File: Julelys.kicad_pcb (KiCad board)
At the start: 4 copper layers, 60 x 53 mm, 85 parts, among them J1 Conn_02x13_Top_Bottom, J10 B3B-XH-A, J11 B3B-XH-A, J12 Conn_01x03_Pin, J2 Conn_01x13, J3 Conn_02x06_Odd_Even, J4 B3B-XH-A, J5 B3B-XH-A, J6 B3B-XH-A, J7 B3B-XH-A, J8 B3B-XH-A, J9 B3B-XH-A, P1 USB_C_Receptacle_USB2.0, SW1 SW_Push, SW2 SW_Push, U1 ESP32-C3-WROOM-02, U2 74HC4051, U3 AMS1117-3.3, U4 BC847BDW1T1G, U5 CP2102N-A02-GQFN28, U6 74AHCT1G125, U7 74AHCT1G125, U8 74AHCT1G125, U9 74AHCT1G125

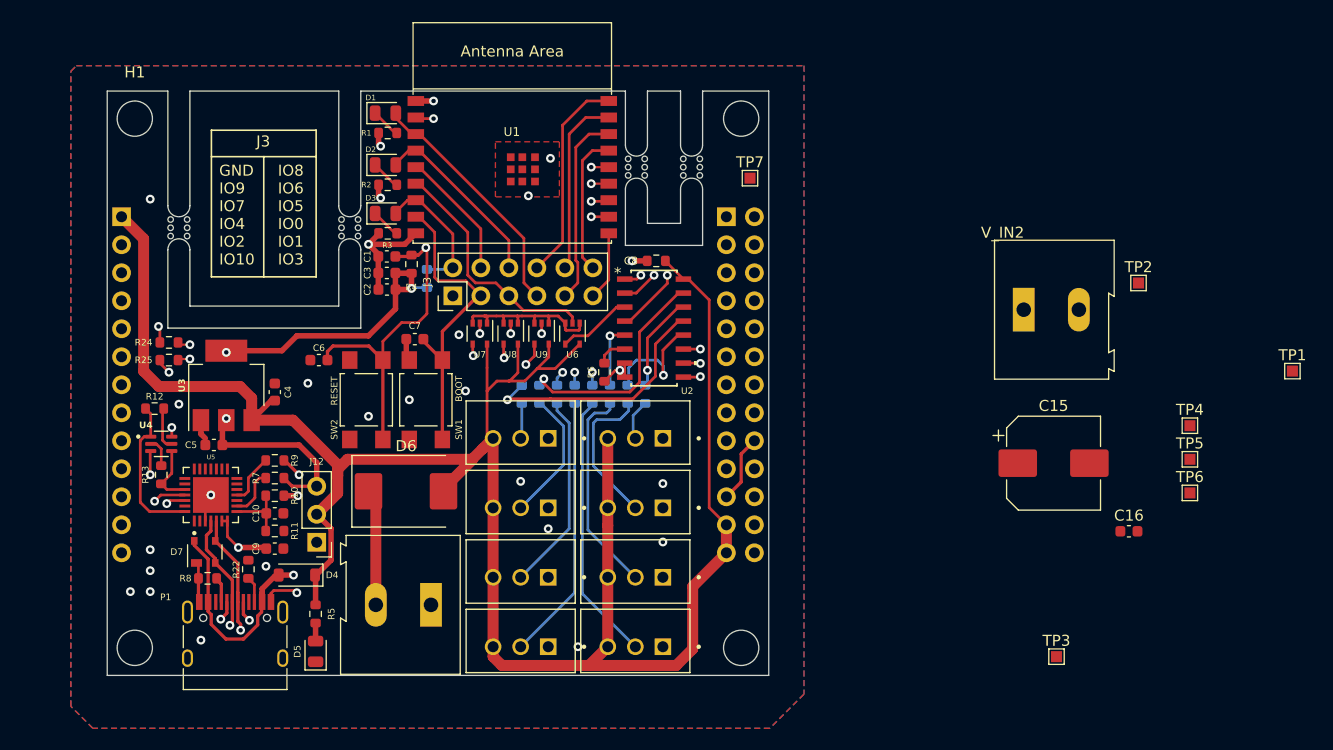
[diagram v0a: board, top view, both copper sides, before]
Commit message: Start v4 layout on Raspberry Pi HAT outline
Clear the v3.1 layout down to a 65x56 mm HAT board outline with the four
M3 mounting holes, ready for fresh placement. Update the schematic and
CLAUDE.md for the Raspberry Pi 40-pin header.

Co-Authored-By: Claude Opus 5.5 <noreply@anthropic.com>
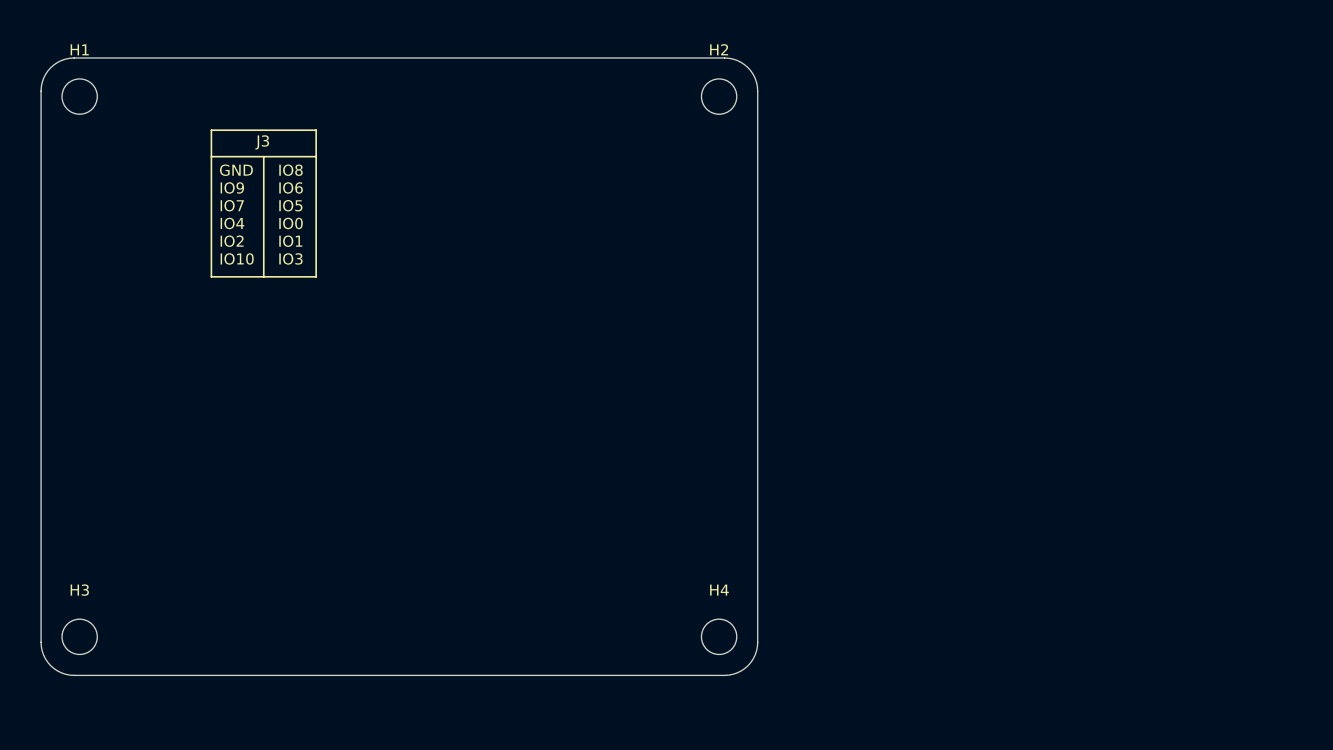
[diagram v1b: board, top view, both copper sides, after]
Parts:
- removed C1: 1uf/16V, Capacitor_SMD:C_0603_1608Metric
- removed C10: 1uF/16V(10%), Capacitor_SMD:C_0603_1608Metric
- removed C15: 470uF, Capacitor_SMD:CP_Elec_8x10
- removed C16: 100nF, Capacitor_SMD:C_0603_1608Metric
- removed C2, C4, C5: 10uf, Capacitor_SMD:C_0603_1608Metric
- removed C3, C6, C7: 0.1uf, Capacitor_SMD:C_0603_1608Metric
- removed C8: 100nf, Resistor_SMD:R_0603_1608Metric
- removed C9: 10uF/25V(20%), Capacitor_SMD:C_0603_1608Metric
- removed D1, D2, D3: LED RED, LED_SMD:LED_0805_2012Metric
- removed D4: 1N5819HW-7-F, Diode_SMD:D_SOD-123
- removed D5: LED GREEN, LED_SMD:LED_0805_2012Metric
- removed D6: SS34, Diode_SMD:D_SMC
- removed D7: SP0503BAHT, Package_TO_SOT_SMD:SOT-143
- removed J1: Conn_02x13_Top_Bottom, Connector_PinSocket_2.54mm:PinSocket_2x13_P2.54mm_Vertical
- removed J10, J11, J4, J5, J6, J7, J8, J9: B3B-XH-A, Connector:JST_B3B-XH-A
- removed J12: Conn_01x03_Pin, Connector_PinHeader_2.54mm:PinHeader_1x03_P2.54mm_Vertical
- removed J2: Conn_01x13, Connector_PinSocket_2.54mm:PinSocket_1x13_P2.54mm_Vertical
- removed J3: Conn_02x06_Odd_Even, Connector_PinHeader_2.54mm:PinHeader_2x06_P2.54mm_Vertical
- removed P1: USB_C_Receptacle_USB2.0, Connector_USB:USB_C_Receptacle_HRO_TYPE-C-31-M-12
- removed R1, R2, R3: 270, Resistor_SMD:R_0603_1608Metric
- removed R10: 22.1K, Resistor_SMD:R_0603_1608Metric
- removed R11: 47.5K, Resistor_SMD:R_0603_1608Metric
- removed R12, R13: 10k, Resistor_SMD:R_0603_1608Metric
- removed R14, R15, R16, R17, R18, R19, R20, R21: 330, Resistor_SMD:R_0603_1608Metric
- removed R22, R8: 5.1K, Resistor_SMD:R_0603_1608Metric
- removed R23, R4, R6, R9: 10K, Resistor_SMD:R_0603_1608Metric
- removed R24, R25: 22, Resistor_SMD:R_0603_1608Metric
- removed R5: 5k1, Resistor_SMD:R_0603_1608Metric
- removed R7: 1K, Resistor_SMD:R_0603_1608Metric
- removed SW1, SW2: SW_Push, Button_Switch_SMD:SW_SPST_TL3305A
- removed TP1: 5V, TestPoint:TestPoint_Pad_1.0x1.0mm
- removed TP2: GND, TestPoint:TestPoint_Pad_1.0x1.0mm
- removed TP3: 3.3V, TestPoint:TestPoint_Pad_1.0x1.0mm
- removed TP4: MOSI, TestPoint:TestPoint_Pad_1.0x1.0mm
- removed TP5: MISO, TestPoint:TestPoint_Pad_1.0x1.0mm
- removed TP6: CLK, TestPoint:TestPoint_Pad_1.0x1.0mm
- removed TP7: CS, TestPoint:TestPoint_Pad_1.0x1.0mm
- removed U1: ESP32-C3-WROOM-02, PCM_Espressif:ESP32-C3-WROOM-02
- removed U2: 74HC4051, 74HC4051D_FOOTPRINT:SOIC16_TOS
- removed U3: AMS1117-3.3, Package_TO_SOT_SMD:SOT-223-3_TabPin2
- removed U4: BC847BDW1T1G, Transistor_Power_Module:SOT65P210X110-6N
- removed U5: CP2102N-A02-GQFN28, Connector_USB:QFN50P500X500X80-29N
- removed U6, U7, U8, U9: 74AHCT1G125, Package_TO_SOT_SMD:SOT-353_SC-70-5
- removed V_IN1, V_IN2: 5V, TerminalBlock:TerminalBlock_Altech_AK300-2_P5.00mm
- removed mouse-bite-2mm-slot (x4): VAL**, footprints:mouse-bite-2mm-slot
- moved H1 5.39 mm to (23.5, 15.5)
- moved H3 5.10 mm to (23.5, 64.5)
- moved H2 2.83 mm to (81.5, 15.5)
- moved H4 2.24 mm to (81.5, 64.5)
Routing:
- net +5V: track 210.7 -> 0.00 mm
- net TXD: track 117.8 -> 0.00 mm, vias 2 -> 0
- net RXD: track 112.6 -> 0.00 mm, vias 2 -> 0
- net +3.3V: track 86.6 -> 0.00 mm, vias 5 -> 0
- net CHIP_UP: track 79.3 -> 0.00 mm, vias 3 -> 0
- net IO9: track 73.2 -> 0.00 mm, vias 1 -> 0
- net GND: track 58.2 -> 0.00 mm, vias 28 -> 0
- net USB_D+: track 54.3 -> 0.00 mm, vias 2 -> 0
- net USB_D-: track 51.0 -> 0.00 mm, vias 2 -> 0
- net IO6: track 39.8 -> 0.00 mm
- net A1: track 37.1 -> 0.00 mm, vias 1 -> 0
- net IO2: track 37.0 -> 0.00 mm
- net CLK: track 35.3 -> 0.00 mm
- net A0: track 34.4 -> 0.00 mm, vias 1 -> 0
- net VBUS: track 28.9 -> 0.00 mm, vias 2 -> 0
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- removed copper zone on B.Cu, net GND
- removed copper zone on F.Cu, net GND
- removed copper zone on In1.Cu, net GND
- removed copper zone on In2.Cu, net GND
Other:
- board size 60 x 53 mm -> 65 x 56 mm
- board text added: "01/2026"
- board text added: "V4.0"
- board text added: "Ω"
- board text removed: "08/2025"
- board text removed: "3.3V"
- board text removed: "5V"
- board text removed: "GND"
- board text removed: "V3.1"
- board text removed: "∑"

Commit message: Add first v4 HAT layout (4 layers, autorouted draft)
- 65x56 mm Raspberry Pi HAT outline, J1 on the bottom at the Pi position
- 4 layers: signal + GND pour on outer layers, In1 GND plane, In2 +5V plane,
  GND stitching vias
- Locked wide power tracks from the screw terminals to the JST outputs and
  to the Pi 5V pins; net classes for power and 3V3
- Address LEDs D1-D3 in one row, power LEDs next to the power input
- Autorouted with Freerouting; 8 connections, 3 edge clearances and the
  silkscreen still need hand work
- Add PWR_FLAG to +5V and GND, remove a stray no-connect (ERC clean)

Co-Authored-By: Claude Opus 5.5 <noreply@anthropic.com>
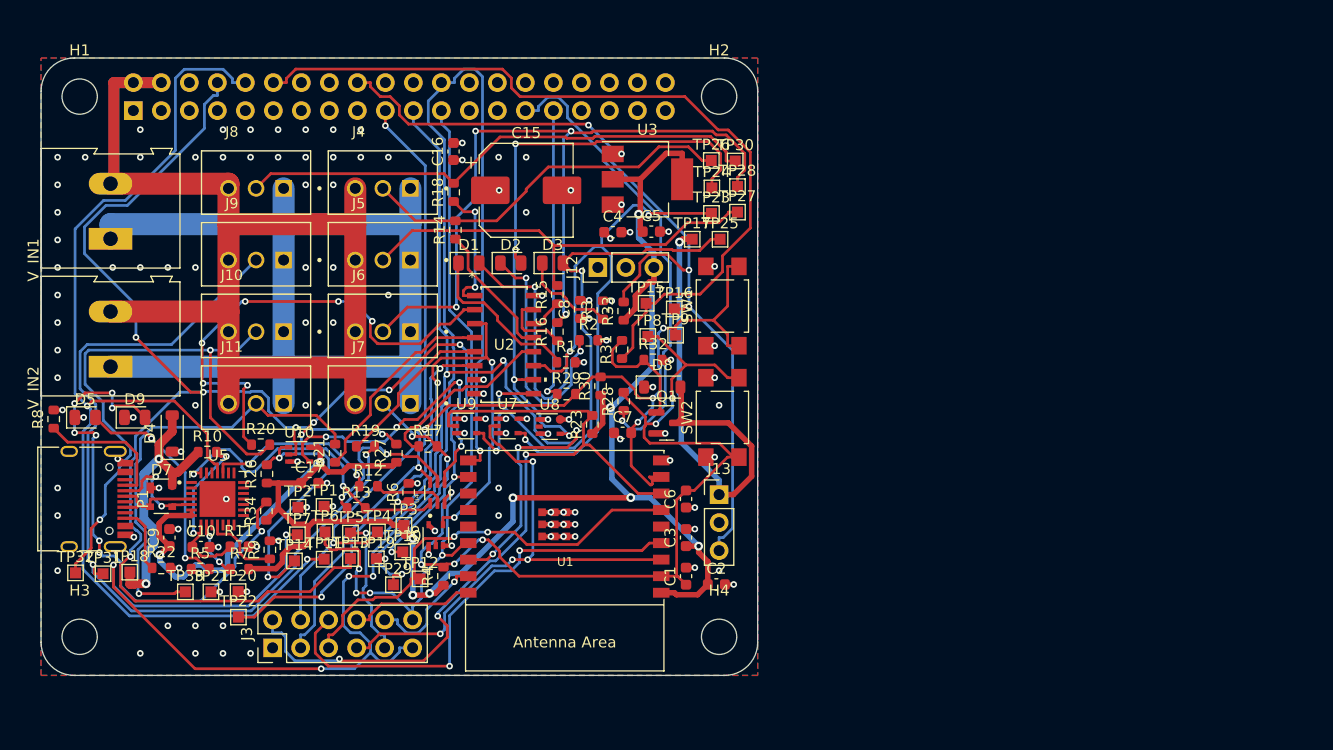
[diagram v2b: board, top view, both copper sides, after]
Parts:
- added C1: 1uf/16V, Capacitor_SMD:C_0603_1608Metric, F.Cu at (78.5, 59.0)
- added C10: 1uF/16V(10%), Capacitor_SMD:C_0603_1608Metric, F.Cu at (34.5, 56.4)
- added C15: 470uF, Capacitor_SMD:CP_Elec_8x10, F.Cu at (64.0, 24.0)
- added C16: 100nF, Capacitor_SMD:C_0603_1608Metric, F.Cu at (57.4, 20.5)
- added C17: 100nF, Capacitor_SMD:C_0603_1608Metric, F.Cu at (44.4, 50.6)
- added C2: 10uf, Capacitor_SMD:C_0603_1608Metric, F.Cu at (81.2, 59.8)
- added C3: 0.1uf, Capacitor_SMD:C_0603_1608Metric, F.Cu at (78.5, 55.5)
- added C4: 10uf, Capacitor_SMD:C_0603_1608Metric, F.Cu at (71.8, 27.8)
- added C5: 10uf, Capacitor_SMD:C_0603_1608Metric, F.Cu at (75.3, 27.8)
- added C6: 0.1uf, Capacitor_SMD:C_0603_1608Metric, F.Cu at (78.5, 52.0)
- added C7: 0.1uf, Capacitor_SMD:C_0603_1608Metric, F.Cu at (72.8, 46.0)
- added C8: 100nf, Resistor_SMD:R_0603_1608Metric, F.Cu at (68.9, 34.8)
- added C9: 10uF/25V(20%), Capacitor_SMD:C_0603_1608Metric, F.Cu at (31.6, 55.5)
- added D1: LED RED, LED_SMD:LED_0805_2012Metric, F.Cu at (58.8, 30.6)
- added D2: LED RED, LED_SMD:LED_0805_2012Metric, F.Cu at (62.6, 30.6)
- added D3: LED RED, LED_SMD:LED_0805_2012Metric, F.Cu at (66.4, 30.6)
- added D4: 1N5819HW-7-F, Diode_SMD:D_SOD-123, F.Cu at (31.9, 46.0)
- added D5: LED GREEN, LED_SMD:LED_0805_2012Metric, F.Cu at (24.0, 44.6)
- added D7: SP0503BAHT, Package_TO_SOT_SMD:SOT-143, F.Cu at (30.9, 51.8)
- added D8: 1N5819HW-7-F, Diode_SMD:D_SOD-123, F.Cu at (76.3, 41.9)
- added D9: LED GREEN, LED_SMD:LED_0805_2012Metric, F.Cu at (28.5, 44.6)
- added J1: Raspberry_Pi_40pin, Connector_PinSocket_2.54mm:PinSocket_2x20_P2.54mm_Vertical, B.Cu at (28.4, 16.8)
- added J10: B3B-XH-A, Connector:JST_B3B-XH-A, F.Cu at (39.5, 36.3)
- added J11: B3B-XH-A, Connector:JST_B3B-XH-A, F.Cu at (39.5, 42.8)
- added J12: Conn_01x03_Pin, Connector_PinHeader_2.54mm:PinHeader_1x03_P2.54mm_Vertical, F.Cu at (70.5, 31.0)
- added J13: FAN, Connector_PinHeader_2.54mm:PinHeader_1x03_P2.54mm_Vertical, F.Cu at (81.5, 51.6)
- added J3: Conn_02x06_Odd_Even, Connector_PinHeader_2.54mm:PinHeader_2x06_P2.54mm_Vertical, F.Cu at (41.0, 65.5)
- added J4: B3B-XH-A, Connector:JST_B3B-XH-A, F.Cu at (51.0, 23.3)
- added J5: B3B-XH-A, Connector:JST_B3B-XH-A, F.Cu at (51.0, 29.8)
- added J6: B3B-XH-A, Connector:JST_B3B-XH-A, F.Cu at (51.0, 36.3)
- added J7: B3B-XH-A, Connector:JST_B3B-XH-A, F.Cu at (51.0, 42.8)
- added J8: B3B-XH-A, Connector:JST_B3B-XH-A, F.Cu at (39.5, 23.3)
- added J9: B3B-XH-A, Connector:JST_B3B-XH-A, F.Cu at (39.5, 29.8)
- added P1: USB_C_Receptacle_USB2.0, Connector_USB:USB_C_Receptacle_HRO_TYPE-C-31-M-12, F.Cu at (23.6, 52.0)
- added Q1: AO3400A, Package_TO_SOT_SMD:SOT-23, F.Cu at (76.8, 45.1)
- added R1: 1K, Resistor_SMD:R_0603_1608Metric, F.Cu at (67.6, 39.6)
- added R10: 22.1K, Resistor_SMD:R_0603_1608Metric, F.Cu at (35.1, 47.7)
- added R11: 47.5K, Resistor_SMD:R_0603_1608Metric, F.Cu at (38.0, 56.3)
- added R12: 10k, Resistor_SMD:R_0603_1608Metric, F.Cu at (49.7, 50.8)
- added R13: 10k, Resistor_SMD:R_0603_1608Metric, F.Cu at (48.6, 52.8)
- added R14: 330, Resistor_SMD:R_0603_1608Metric, F.Cu at (57.6, 27.6)
- added R15: 330, Resistor_SMD:R_0603_1608Metric, F.Cu at (66.8, 33.5)
- added R16: 330, Resistor_SMD:R_0603_1608Metric, F.Cu at (66.8, 36.8)
- added R17: 330, Resistor_SMD:R_0603_1608Metric, F.Cu at (55.1, 47.2)
- added R18: 330, Resistor_SMD:R_0603_1608Metric, F.Cu at (57.4, 24.2)
- added R19: 330, Resistor_SMD:R_0603_1608Metric, F.Cu at (49.4, 47.2)
- added R2: 1K, Resistor_SMD:R_0603_1608Metric, F.Cu at (69.7, 37.6)
- added R20: 330, Resistor_SMD:R_0603_1608Metric, F.Cu at (39.9, 47.1)
- added R21: 330, Resistor_SMD:R_0603_1608Metric, F.Cu at (46.7, 47.8)
- added R22: 5.1K, Resistor_SMD:R_0603_1608Metric, F.Cu at (30.9, 58.2)
- added R23: 10K, Resistor_SMD:R_0603_1608Metric, F.Cu at (70.0, 45.2)
- added R26: 10K, Resistor_SMD:R_0603_1608Metric, F.Cu at (40.5, 49.7)
- added R27: 10K, Resistor_SMD:R_0603_1608Metric, F.Cu at (52.2, 47.8)
- added R28: 1K, Resistor_SMD:R_0603_1608Metric, F.Cu at (72.8, 43.1)
- added R29: 1K, Resistor_SMD:R_0603_1608Metric, F.Cu at (67.6, 42.5)
- added R3: 1K, Resistor_SMD:R_0603_1608Metric, F.Cu at (71.0, 34.9)
- added R30: 10K, Resistor_SMD:R_0603_1608Metric, F.Cu at (70.8, 41.8)
- added R31: 100, Resistor_SMD:R_0603_1608Metric, F.Cu at (72.7, 38.4)
- added R32: 100K, Resistor_SMD:R_0603_1608Metric, F.Cu at (75.5, 39.4)
- added R33: 10K, Resistor_SMD:R_0603_1608Metric, F.Cu at (72.8, 35.0)
- added R34: 1K, Resistor_SMD:R_0603_1608Metric, F.Cu at (40.4, 53.1)
- added R4: 10K, Resistor_SMD:R_0603_1608Metric, F.Cu at (56.5, 59.0)
- added R5: 5k1, Resistor_SMD:R_0603_1608Metric, F.Cu at (34.4, 58.4)
- added R6: 10K, Resistor_SMD:R_0603_1608Metric, F.Cu at (53.3, 51.4)
- added R7: 1K, Resistor_SMD:R_0603_1608Metric, F.Cu at (38.0, 58.4)
- added R8: 5.1K, Resistor_SMD:R_0603_1608Metric, F.Cu at (21.1, 44.8)
- added R9: 10K, Resistor_SMD:R_0603_1608Metric, F.Cu at (40.8, 56.6)
- added SW1: SW_Push, Button_Switch_SMD:SW_SPST_TL3305A, F.Cu at (81.8, 34.5)
- added SW2: SW_Push, Button_Switch_SMD:SW_SPST_TL3305A, F.Cu at (81.8, 44.6)
- added TP1: 5V, TestPoint:TestPoint_Pad_1.0x1.0mm, F.Cu at (45.7, 52.7)
- added TP10: RXD, TestPoint:TestPoint_Pad_1.0x1.0mm, F.Cu at (52.8, 56.8)
- added TP11: TXD, TestPoint:TestPoint_Pad_1.0x1.0mm, F.Cu at (45.7, 57.5)
- added TP12: LED_DATA, TestPoint:TestPoint_Pad_1.0x1.0mm, F.Cu at (54.4, 59.2)
- added TP13: PI_TX, TestPoint:TestPoint_Pad_1.0x1.0mm, F.Cu at (48.1, 57.4)
- added TP14: USB_TX, TestPoint:TestPoint_Pad_1.0x1.0mm, F.Cu at (43.0, 57.6)
- added TP15: FAN_PWM, TestPoint:TestPoint_Pad_1.0x1.0mm, F.Cu at (74.9, 34.2)
- added TP16: FAN_TACH, TestPoint:TestPoint_Pad_1.0x1.0mm, F.Cu at (77.4, 34.8)
- added TP17: FAN_N, TestPoint:TestPoint_Pad_1.0x1.0mm, F.Cu at (79.1, 28.4)
- added TP18: VBUS, TestPoint:TestPoint_Pad_1.0x1.0mm, F.Cu at (28.1, 58.6)
- added TP19: GND, TestPoint:TestPoint_Pad_1.0x1.0mm, F.Cu at (50.4, 57.4)
- added TP2: GND, TestPoint:TestPoint_Pad_1.0x1.0mm, F.Cu at (43.3, 52.8)
- added TP20: GND, TestPoint:TestPoint_Pad_1.0x1.0mm, F.Cu at (37.9, 60.4)
- added TP21: GND, TestPoint:TestPoint_Pad_1.0x1.0mm, F.Cu at (35.4, 60.4)
- added TP22: DATA, TestPoint:TestPoint_Pad_1.0x1.0mm, F.Cu at (37.9, 62.7)
- added TP23: AS0, TestPoint:TestPoint_Pad_1.0x1.0mm, F.Cu at (80.8, 26.1)
- added TP24: AS1, TestPoint:TestPoint_Pad_1.0x1.0mm, F.Cu at (80.8, 23.8)
- added TP25: AS2, TestPoint:TestPoint_Pad_1.0x1.0mm, F.Cu at (81.6, 28.4)
- added TP26: CH1, TestPoint:TestPoint_Pad_1.0x1.0mm, F.Cu at (80.8, 21.3)
- added TP27: CH2, TestPoint:TestPoint_Pad_1.0x1.0mm, F.Cu at (83.2, 26.0)
- added TP28: CH3, TestPoint:TestPoint_Pad_1.0x1.0mm, F.Cu at (83.2, 23.7)
- added TP29: CH4, TestPoint:TestPoint_Pad_1.0x1.0mm, F.Cu at (52.0, 59.8)
- added TP3: 3.3V, TestPoint:TestPoint_Pad_1.0x1.0mm, F.Cu at (52.9, 54.4)
- added TP30: CH5, TestPoint:TestPoint_Pad_1.0x1.0mm, F.Cu at (83.0, 21.3)
- added TP31: CH6, TestPoint:TestPoint_Pad_1.0x1.0mm, F.Cu at (25.6, 58.8)
- added TP32: CH7, TestPoint:TestPoint_Pad_1.0x1.0mm, F.Cu at (23.1, 58.7)
- added TP33: CH8, TestPoint:TestPoint_Pad_1.0x1.0mm, F.Cu at (33.1, 60.4)
- added TP4: MOSI, TestPoint:TestPoint_Pad_1.0x1.0mm, F.Cu at (50.5, 55.0)
- added TP5: MISO, TestPoint:TestPoint_Pad_1.0x1.0mm, F.Cu at (48.1, 55.1)
- added TP6: CLK, TestPoint:TestPoint_Pad_1.0x1.0mm, F.Cu at (45.8, 55.0)
- added TP7: CS, TestPoint:TestPoint_Pad_1.0x1.0mm, F.Cu at (43.3, 55.2)
- added TP8: EN, TestPoint:TestPoint_Pad_1.0x1.0mm, F.Cu at (75.0, 37.3)
- added TP9: BOOT, TestPoint:TestPoint_Pad_1.0x1.0mm, F.Cu at (77.6, 37.1)
- added U1: ESP32-C3-WROOM-02, PCM_Espressif:ESP32-C3-WROOM-02, F.Cu at (67.5, 54.6)
- added U10: 74LVC1G08, Package_TO_SOT_SMD:SOT-353_SC-70-5, F.Cu at (43.4, 48.0)
- added U2: 74HC4051, 74HC4051D_FOOTPRINT:SOIC16_TOS, F.Cu at (62.0, 38.0)
- added U3: AMS1117-3.3, Package_TO_SOT_SMD:SOT-223-3_TabPin2, F.Cu at (75.0, 23.0)
- added U4: BC847BDW1T1G, Transistor_Power_Module:SOT65P210X110-6N, F.Cu at (55.9, 51.4)
- added U5: CP2102N-A02-GQFN28, Connector_USB:QFN50P500X500X80-29N, F.Cu at (36.0, 52.0)
- added U6: 74AHCT1G125, Package_TO_SOT_SMD:SOT-353_SC-70-5, F.Cu at (55.8, 55.3)
- added U7: 74AHCT1G125, Package_TO_SOT_SMD:SOT-353_SC-70-5, F.Cu at (62.3, 45.4)
- added U8: 74AHCT1G125, Package_TO_SOT_SMD:SOT-353_SC-70-5, F.Cu at (66.1, 45.4)
- added U9: 74AHCT1G125, Package_TO_SOT_SMD:SOT-353_SC-70-5, F.Cu at (58.6, 45.4)
- added V_IN1: 5V, TerminalBlock:TerminalBlock_Altech_AK300-2_P5.00mm, F.Cu at (26.3, 28.4)
- added V_IN2: 5V, TerminalBlock:TerminalBlock_Altech_AK300-2_P5.00mm, F.Cu at (26.3, 40.0)
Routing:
- net +3.3V: track 0.00 -> 173.3 mm, vias 0 -> 10
- net CS: track 0.00 -> 158.9 mm, vias 0 -> 6
- net GND: track 0.00 -> 144.7 mm, vias 0 -> 115
- net +5V: track 0.00 -> 122.0 mm, vias 0 -> 14
- net PI_TX: track 0.00 -> 109.4 mm, vias 0 -> 5
- net TXD: track 0.00 -> 100.0 mm, vias 0 -> 2
- net IO2: track 0.00 -> 94.6 mm, vias 0 -> 6
- net IO9: track 0.00 -> 84.6 mm, vias 0 -> 5
- net CHIP_UP: track 0.00 -> 81.5 mm, vias 0 -> 6
- net FAN_TACH: track 0.00 -> 78.9 mm, vias 0 -> 3
- net /CH6: track 0.00 -> 77.7 mm, vias 0 -> 2
- net /AS0: track 0.00 -> 77.3 mm, vias 0 -> 4
- net FAN_PWM: track 0.00 -> 73.6 mm
- net A2: track 0.00 -> 72.9 mm, vias 0 -> 3
- net /CH3: track 0.00 -> 71.0 mm, vias 0 -> 4
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- added copper zone on In2.Cu, net +5V
- added copper zone on B.Cu, net GND
- added copper zone on F.Cu, net GND
- added copper zone on In1.Cu, net GND
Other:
- board text removed: "GND IO9 IO7 IO4 IO2 IO10"
- board text removed: "IO8 IO6 IO5 IO0 IO1 IO3"
- board text removed: "J3"

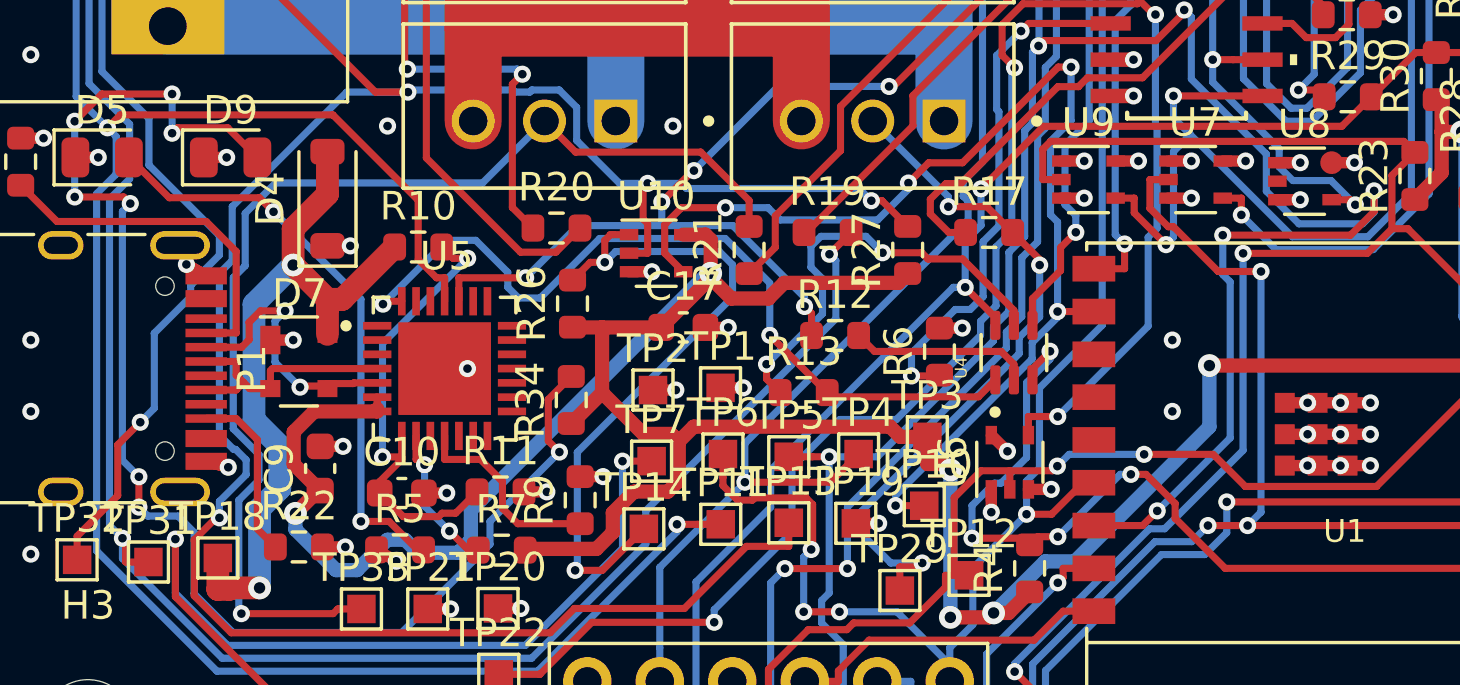
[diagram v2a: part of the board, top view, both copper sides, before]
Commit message: Route 3 more v4 connections, move board to KiCad 10 format
- Route USB D- between the P1 pads, U5 GND pin 3 and A1 to U8
- Board file saved in KiCad 10 format; zones refilled
- 5 connections left for interactive routing (TXD, IO6, USB_TX, 2x VBUS)
- Ignore KiCad 10's .history/ directory

Co-Authored-By: Claude Opus 5.5 <noreply@anthropic.com>
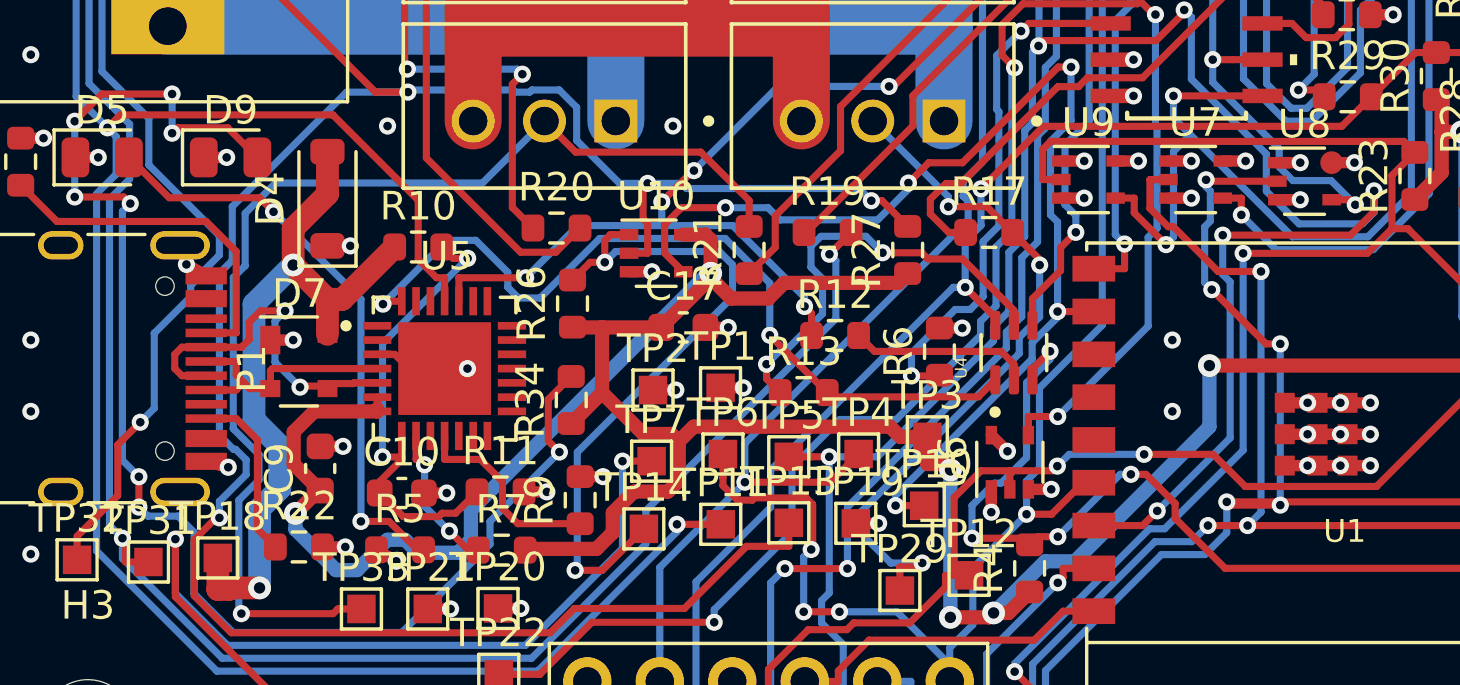
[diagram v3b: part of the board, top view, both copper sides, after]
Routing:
- net A1: track 43.3 -> 60.7 mm, vias 2 -> 6
- net Net-(U5-D-): track 9.74 -> 12.6 mm
- net GND: track 144.7 -> 147.3 mm
